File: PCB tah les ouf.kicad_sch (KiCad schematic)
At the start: 5 parts, among them J1 USB_C_Receptacle_USB2.0_16P, U1 ESP32-S3-WROOM-1

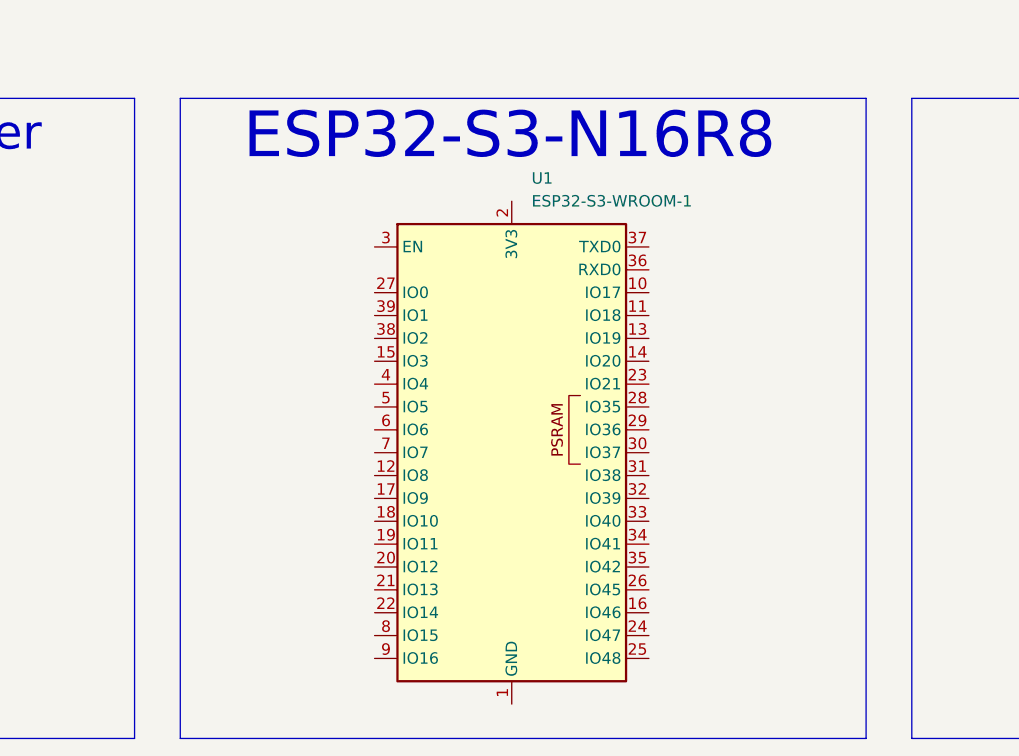
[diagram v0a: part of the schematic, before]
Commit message: Ajustement TMC
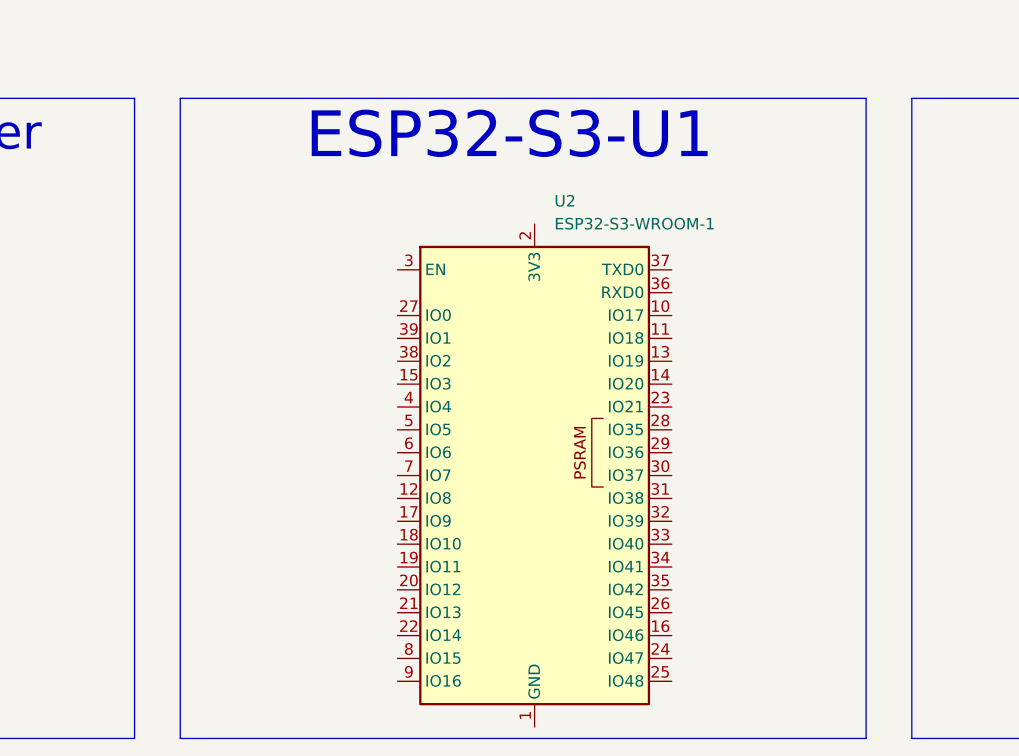
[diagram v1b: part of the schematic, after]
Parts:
- removed U1: ESP32-S3-WROOM-1, RF_Module:ESP32-S3-WROOM-1, symbol RF_Module:ESP32-S3-WROOM-1
- added U2: ESP32-S3-WROOM-1, RF_Module:ESP32-S3-WROOM-1U, symbol RF_Module:ESP32-S3-WROOM-1
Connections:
- new net: U2.1 (GND), U2.40 (GND), U2.41 (GND)
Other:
- note added: "ESP32-S3-U1"
- note removed: "ESP32-S3-N16R8"
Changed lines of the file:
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@@
 		)
 	)
-	(text "ESP32-S3-N16R8"
+	(text "ESP32-S3-U1"
 		(exclude_from_sim no)
 		(at 219.456 27.178 0)
@@
 			)
 			(justify left bottom)
+		)
+	)
+	(symbol
+		(lib_id "RF_Module:ESP32-S3-WROOM-1")
+		(at 222.25 64.77 0)
+		(unit 1)
+		(exclude_from_sim no)
+		(in_bom yes)
+		(on_board yes)
+		(dnp no)
+		(fields_autoplaced yes)
+		(property "Reference" "U2"
+			(at 224.4441 34.29 0)
+			(effects
+				(font
+					(size 1.27 1.27)
+				)
+				(justify left)
+			)
+		)
+		(property "Value" "ESP32-S3-WROOM-1"
+			(at 224.4441 36.83 0)
+			(effects
+				(font
+					(size 1.27 1.27)
+				)
+				(justify left)
+			)
+		)
+		(property "Footprint" "RF_Module:ESP32-S3-WROOM-1U"
+			(at 222.25 62.23 0)
+			(effects
+				(font
+					(size 1.27 1.27)
+				)
+				(hide yes)
+			)
+		)
+		(property "Datasheet" "https://www.espressif.com/sites/default/files/documentation/esp32-s3-wroom-1_wroom-1u_datasheet_en.pdf"
+			(at 222.25 64.77 0)
+			(effects
+				(font
+					(size 1.27 1.27)
+				)
+				(hide yes)
+			)
+		)
+		(property "Description" "RF Module, ESP32-S3 SoC, Wi-Fi 802.11b/g/n, Bluetooth, BLE, 32-bit, 3.3V, onboard antenna, SMD"
+			(at 222.25 64.77 0)
+			(effects
+				(font
+					(size 1.27 1.27)
+				)
+				(hide yes)
+			)
+		)
+		(pin "6"
+		)
+		(pin "9"
+		)
+		(pin "1"
+		)
+		(pin "20"
+		)
+		(pin "10"
+		)
+		(pin "30"
+		)
+		(pin "37"
+		)
+		(pin "21"
+		)
+		(pin "28"
+		)
+		(pin "38"
+		)
+		(pin "31"
+		)
+		(pin "19"
+		)
+		(pin "16"
+		)
+		(pin "3"
+		)
+		(pin "33"
+		)
+		(pin "17"
+		)
+		(pin "36"
+		)
+		(pin "8"
+		)
+		(pin "2"
+		)
+		(pin "11"
+		)
+		(pin "23"
+		)
+		(pin "18"
+		)
+		(pin "5"
+		)
+		(pin "14"
+		)
+		(pin "7"
+		)
+		(pin "15"
+		)
+		(pin "12"
+		)
+		(pin "22"
+		)
+		(pin "13"
+		)
+		(pin "24"
+		)
+		(pin "25"
+		)
+		(pin "40"
+		)
+		(pin "27"
+		)
+		(pin "41"
+		)
+		(pin "4"
+		)
+		(pin "34"
+		)
+		(pin "35"
+		)
+		(pin "29"
+		)
+		(pin "32"
+		)
+		(pin "39"
+		)
+		(pin "26"
+		)
+		(instances
+			(project "PCB tah les ouf"
+				(path "/ea97f20c-9bc4-49f4-bc03-d8d68656df8b"
+					(reference "U2")
+					(unit 1)
+				)
+			)
 		)
 	)
@@
 					(unit 1)
 				)
-			)
-		)
-	)
-	(symbol
-		(lib_id "RF_Module:ESP32-S3-WROOM-1")
-		(at 219.71 62.23 0)
-		(unit 1)
-		(exclude_from_sim no)
-		(in_bom yes)
-		(on_board yes)
-		(dnp no)
-		(fields_autoplaced yes)
-		(property "Reference" "U1"
-			(at 221.9041 31.75 0)
-			(effects
-				(font
-					(size 1.27 1.27)
-				)
-				(justify left)
-			)
-		)
-		(property "Value" "ESP32-S3-WROOM-1"
-			(at 221.9041 34.29 0)
-			(effects
-				(font
-					(size 1.27 1.27)
-				)
-				(justify left)
-			)
-		)
-		(property "Footprint" "RF_Module:ESP32-S3-WROOM-1"
-			(at 219.71 59.69 0)
-			(effects
-				(font
-					(size 1.27 1.27)
-				)
-				(hide yes)
-			)
-		)
-		(property "Datasheet" "https://www.espressif.com/sites/default/files/documentation/esp32-s3-wroom-1_wroom-1u_datasheet_en.pdf"
-			(at 219.71 62.23 0)
-			(effects
-				(font
-					(size 1.27 1.27)
-				)
-				(hide yes)
-			)
-		)
-		(property "Description" "RF Module, ESP32-S3 SoC, Wi-Fi 802.11b/g/n, Bluetooth, BLE, 32-bit, 3.3V, onboard antenna, SMD"
-			(at 219.71 62.23 0)
-			(effects
-				(font
-					(size 1.27 1.27)
-				)
-				(hide yes)
-			)
-		)
-		(pin "41"
-		)
-		(pin "5"
-		)
-		(pin "39"
-		)
-		(pin "6"
-		)
-		(pin "4"
-		)
-		(pin "9"
-		)
-		(pin "8"
-		)
-		(pin "40"
-		)
-		(pin "7"
-		)
-		(pin "14"
-		)
-		(pin "36"
-		)
-		(pin "33"
-		)
-		(pin "21"
-		)
-		(pin "37"
-		)
-		(pin "35"
-		)
-		(pin "38"
-		)
-		(pin "3"
-		)
-		(pin "1"
-		)
-		(pin "18"
-		)
-		(pin "2"
-		)
-		(pin "15"
-		)
-		(pin "28"
-		)
-		(pin "30"
-		)
-		(pin "11"
-		)
-		(pin "25"
-		)
-		(pin "17"
-		)
-		(pin "26"
-		)
-		(pin "20"
-		)
-		(pin "10"
-		)
-		(pin "22"
-		)
-		(pin "23"
-		)
-		(pin "24"
-		)
-		(pin "12"
-		)
-		(pin "29"
-		)
-		(pin "13"
-		)
-		(pin "27"
-		)
-		(pin "16"
-		)
-		(pin "19"
-		)
-		(pin "31"
-		)
-		(pin "32"
-		)
-		(pin "34"
-		)
-		(instances
-			(project "PCB tah les ouf"
-				(path "/ea97f20c-9bc4-49f4-bc03-d8d68656df8b"
-					(reference "U1")
-					(unit 1)
-				)

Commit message: AJOUT driver stepper
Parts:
- added BOOT, BUILTIN, RESET: SW_MEC_5E, Button_Switch_SMD:SW_MEC_5GSH9, symbol Switch:SW_MEC_5E
- added BZ1: Buzzer, symbol Device:Buzzer
- added C2, C3: 0.1uF, symbol Device:C
- added R3: 10k, symbol Device:R
- added U2, U3, U4, U5: TMC2209_SILENTSTEPSTICK, TMC2209:MODULE_TMC2209_SILENTSTEPSTICK, symbol TMC2209_SILENTSTEPSTICK:TMC2209_SILENTSTEPSTICK
- renumbered U2 to U1
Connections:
- net GND: now also U1.1 (GND), U1.40 (GND), U1.41 (GND), BOOT.1, BOOT.2, BZ1.2 (-), C2.2, C3.2, RESET.1, RESET.2, U2.1 (GND), U2.7 (GND), U3.1 (GND), U3.7 (GND), U4.1 (GND), U4.7 (GND), U5.1 (GND), U5.7 (GND)
- net ESP32_EN: now reaches U1.3 (EN)
- net ESP32_EN: now also C2.1, R3.2, RESET.3 (K), RESET.4 (A)
- new net 3V3: R3.1
- new net GPIO0: BOOT.3 (K), BOOT.4 (A), C3.1
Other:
- note added: "Buttons x3"
- note added: "Buzzer"
- note added: "I²C"
- note added: "LEDs x3"
- note added: "LiDAR"
- note added: "NEMA 17 Drivers"
- note removed: "USB A"
- moved on the sheet: U1

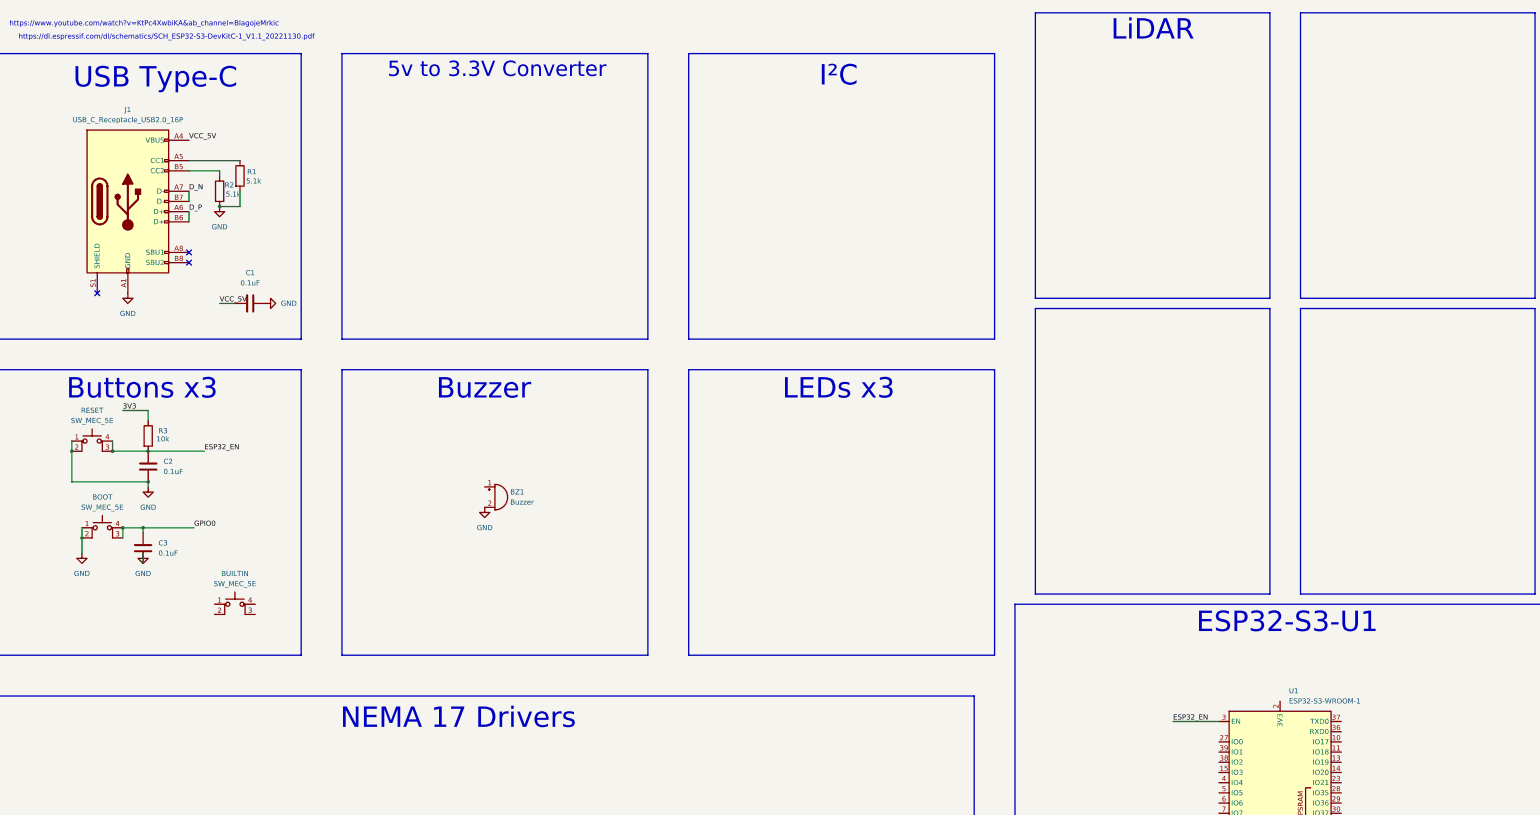
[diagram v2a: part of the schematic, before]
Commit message: Fix problem / ESD Protection
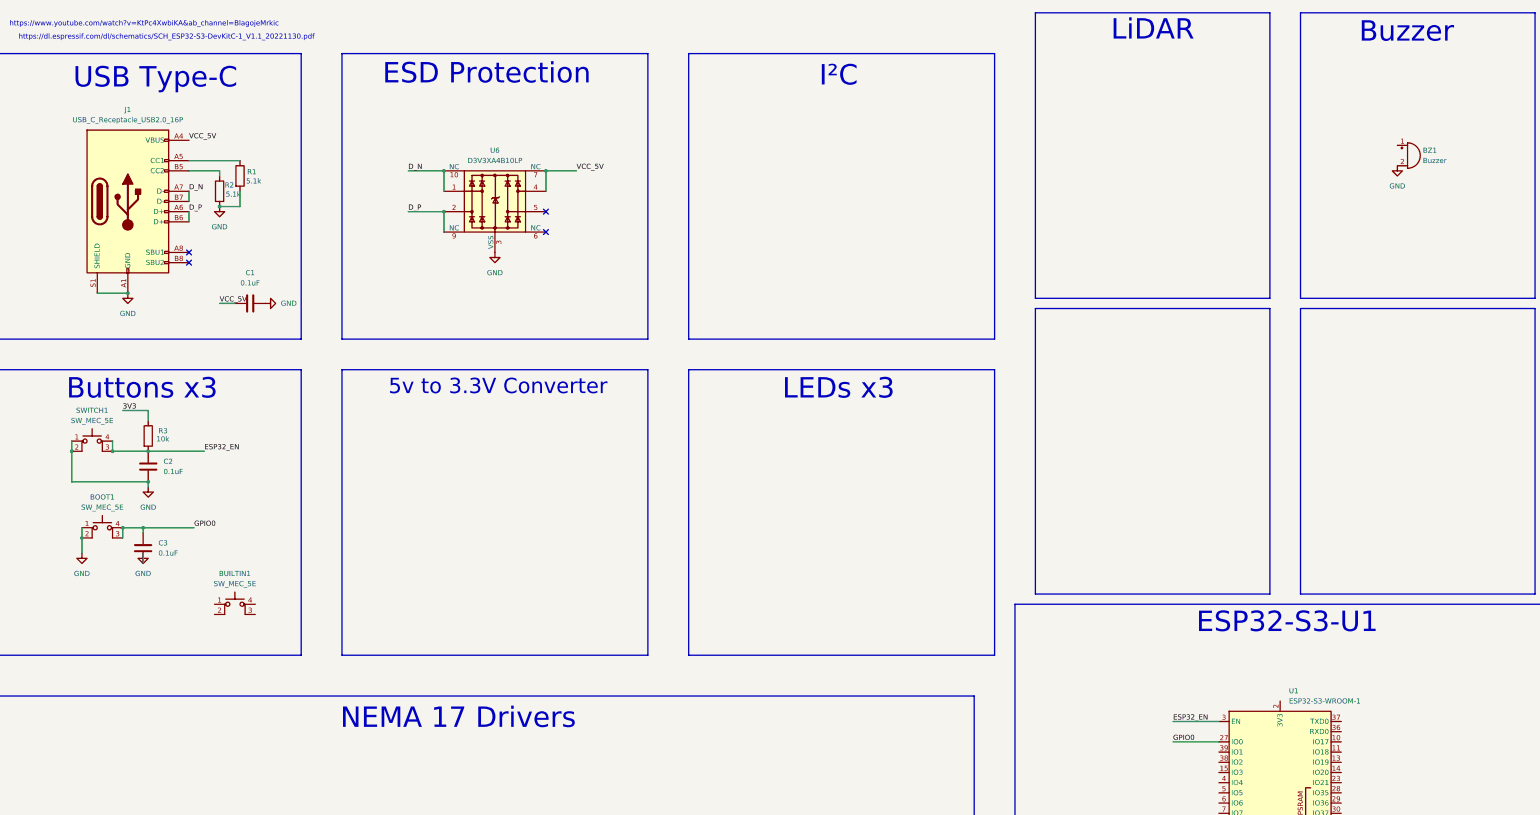
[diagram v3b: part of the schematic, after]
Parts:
- removed RESET: SW_MEC_5E, Button_Switch_SMD:SW_MEC_5GSH9, symbol Switch:SW_MEC_5E
- added SWITCH1: SW_MEC_5E, Button_Switch_THT:SW_PUSH_6mm_H4.3mm, symbol Switch:SW_MEC_5E
- added U6: D3V3XA4B10LP, Package_DFN_QFN:Diodes_UDFN-10_1.0x2.5mm_P0.5mm, symbol Power_Protection:D3V3XA4B10LP
- BOOT1: renamed from BOOT; footprint Button_Switch_SMD:SW_MEC_5GSH9 -> Button_Switch_THT:SW_PUSH_6mm_H4.3mm
- BUILTIN1: renamed from BUILTIN; footprint Button_Switch_SMD:SW_MEC_5GSH9 -> Button_Switch_THT:SW_PUSH_6mm_H4.3mm
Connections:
- net D_N: now also U6.1, U6.10 (NC)
- net D_P: now also U6.2, U6.9 (NC)
- net ESP32_EN: now also SWITCH1.3 (K), SWITCH1.4 (A)
- net GND: now also J1.S1 (SHIELD), SWITCH1.1, SWITCH1.2, U6.3 (VSS), U6.8 (VSS)
- net GPIO0: now also U1.27 (IO0)
- net VCC_5V: now also U6.4, U6.7 (NC)
- no-connect marks 3 -> 4
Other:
- note added: "ESD Protection"
- moved on the sheet: BZ1

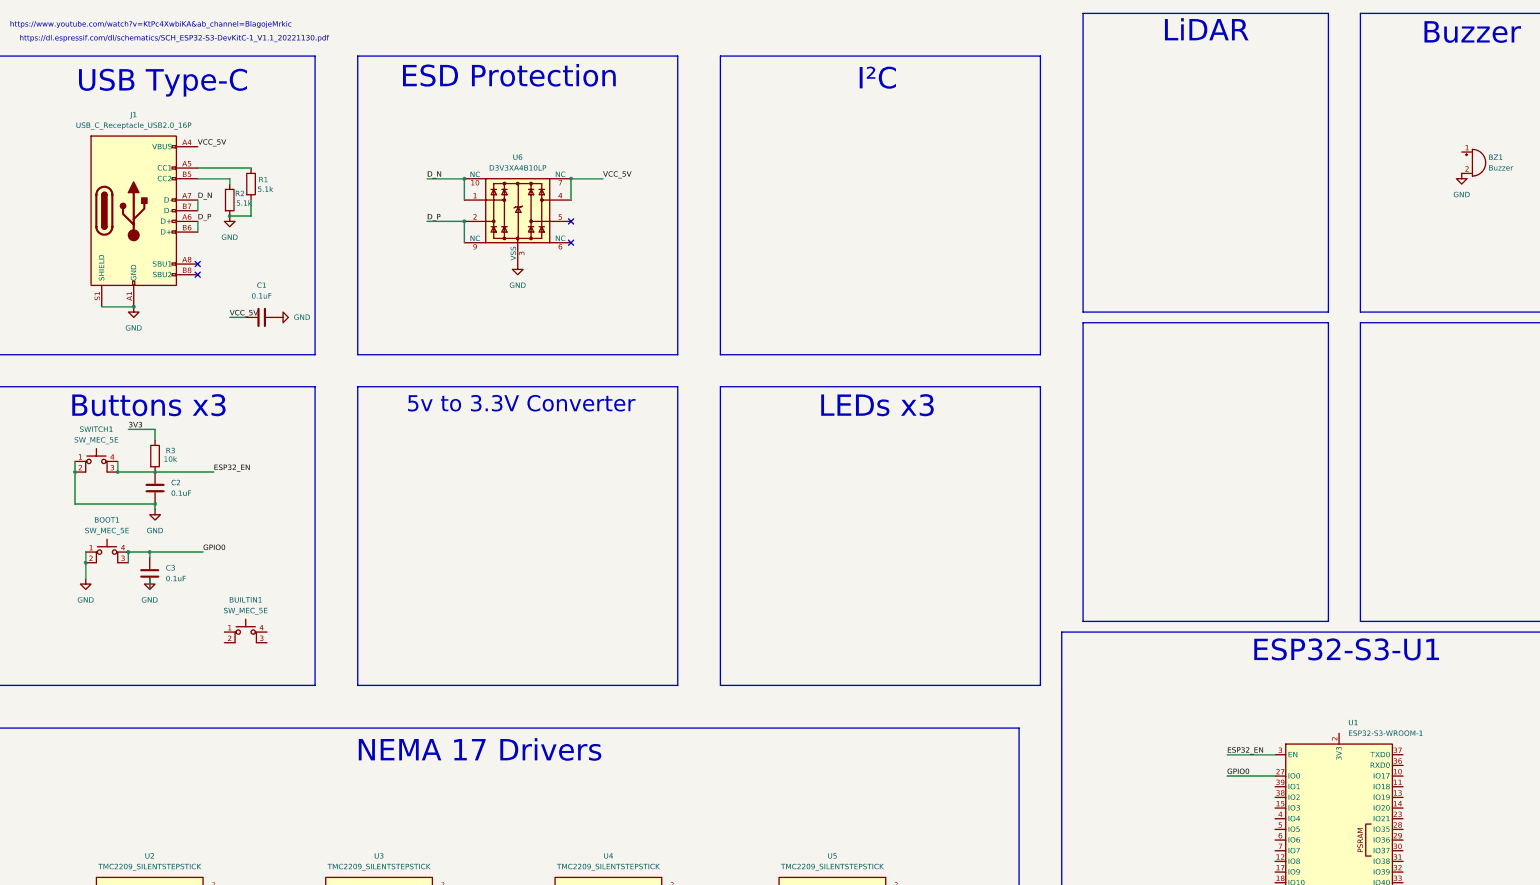
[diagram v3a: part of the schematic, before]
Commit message: correction problemes
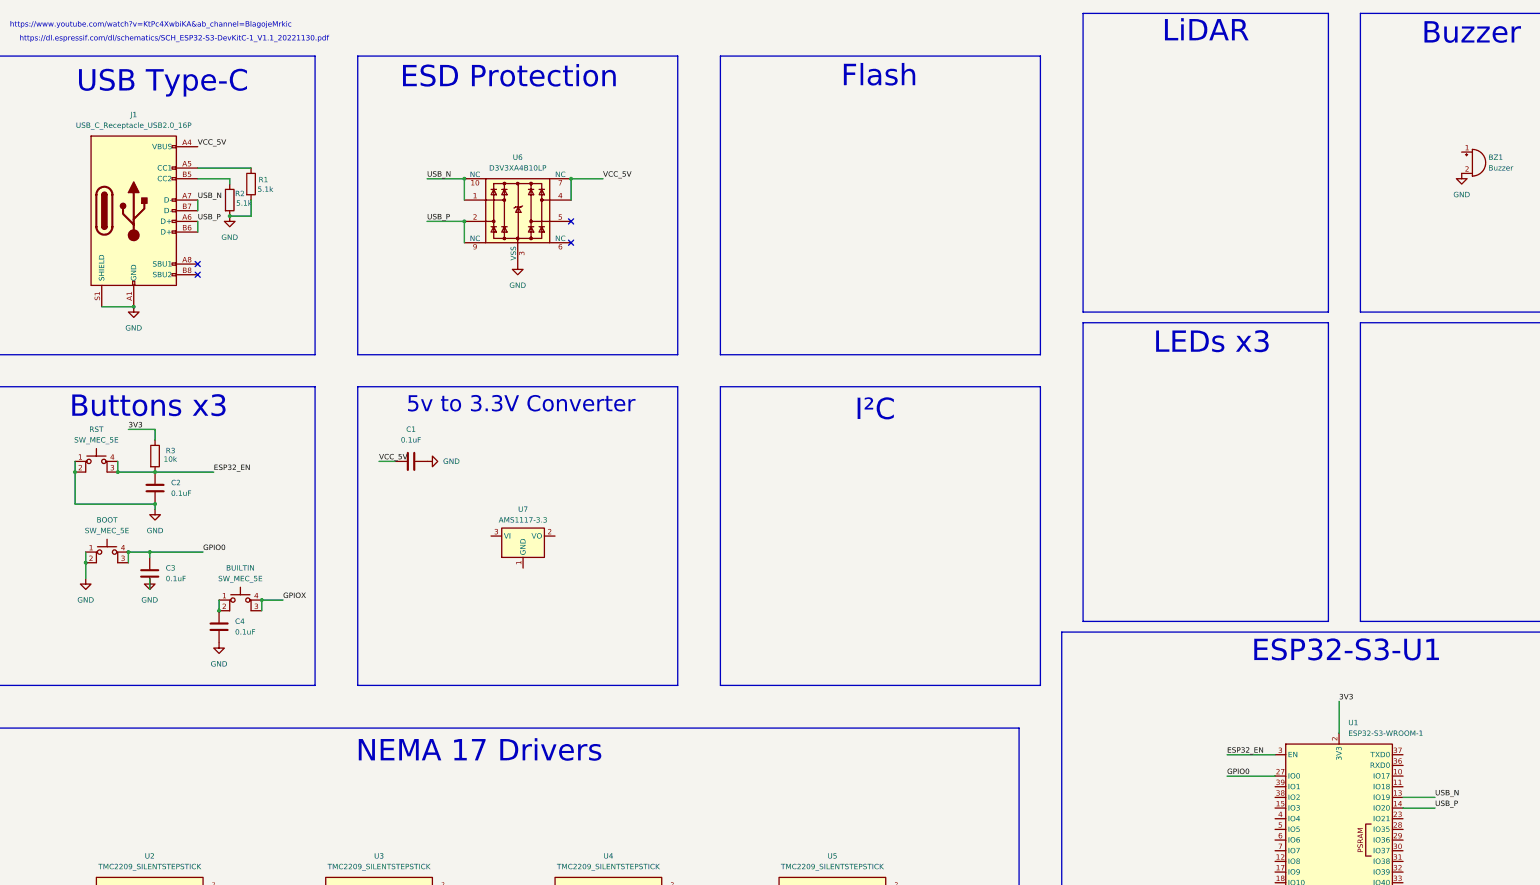
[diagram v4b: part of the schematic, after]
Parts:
- added C4: 0.1uF, symbol Device:C
- added U7: AMS1117-3.3, Package_TO_SOT_SMD:SOT-223-3_TabPin2, symbol Regulator_Linear:AMS1117-3.3
- renumbered BOOT1 to BOOT, BUILTIN1 to BUILTIN, SWITCH1 to RST
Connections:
- net D_N is gone; now on net USB_N: J1.A7 (D-), J1.B7 (D-), U6.1, U6.10 (NC)
- net D_P is gone; now on net USB_P: J1.A6 (D+), J1.B6 (D+), U6.2, U6.9 (NC)
- net 3V3: now also U1.2 (3V3)
- net GND: now also C4.2
- net USB_N: now reaches U1.13 (IO19)
- net USB_P: now reaches U1.14 (IO20)
- net at BUILTIN.1: now also BUILTIN.2, C4.1
- net GPIOX: now reaches BUILTIN.3 (K)
- net GPIOX: now also BUILTIN.4 (A)
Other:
- note added: "Flash"
- moved on the sheet: BUILTIN, C1
